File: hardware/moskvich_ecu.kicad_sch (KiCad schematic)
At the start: 42 parts, among them J1 Power, J2 Sensors, Q1 ISL9V3040P3, Q2 BC847B, U1 ESP32-C3-Zero, U2 AP63205WU-7, U3 SN74HCT123D

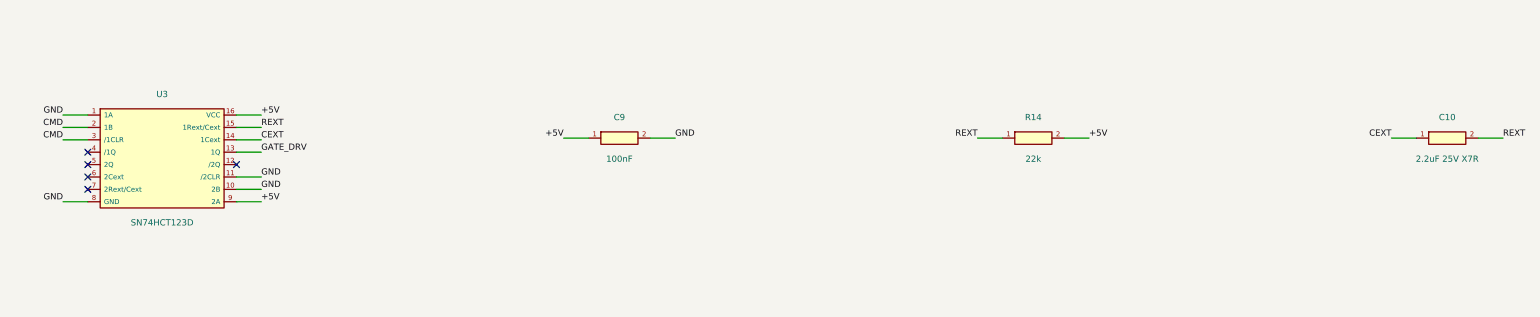
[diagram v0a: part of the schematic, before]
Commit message: hardware: switch the coil guard to CD74HCT221M96 (same pinout, tW = 0.7 R C), R14 = 15k
Co-Authored-By: Claude Sonnet 5.5 <noreply@anthropic.com>
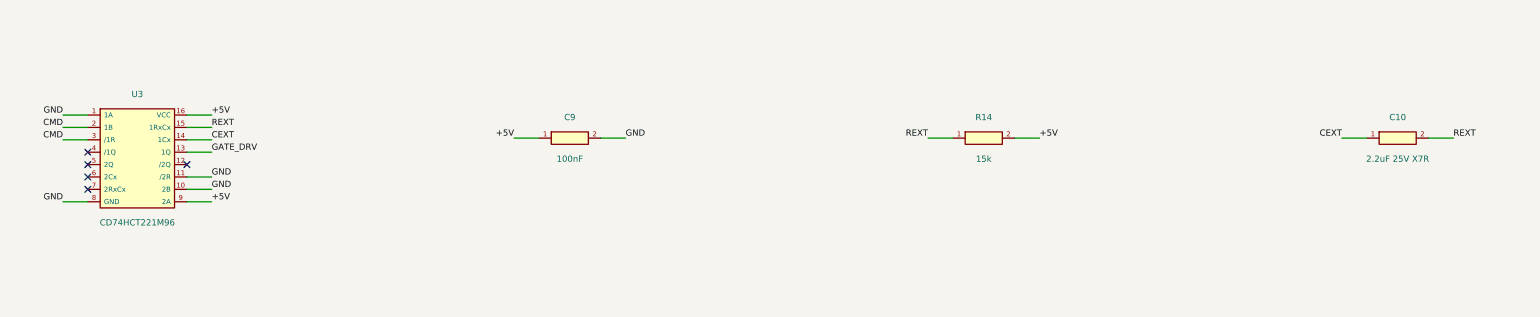
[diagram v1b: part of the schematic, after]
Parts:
- R14: value 22k -> 15k
- U3: value SN74HCT123D -> CD74HCT221M96
